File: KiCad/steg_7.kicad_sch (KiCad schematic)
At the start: 16 parts, among them U1 W65C02S, U2 LCD, U3 W65C22, U4 74HC00

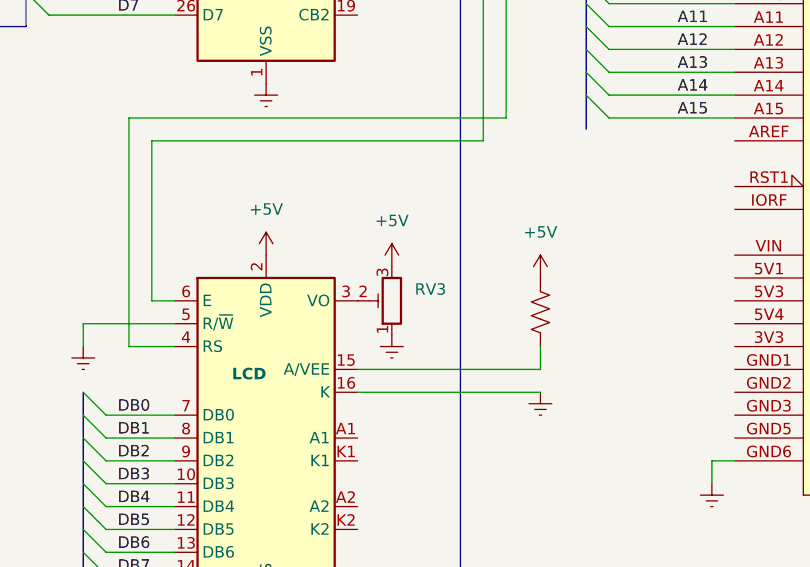
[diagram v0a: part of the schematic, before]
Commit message: Revert "Add trim potentiometer symbol and update power symbols in schematics"
This reverts commit c4bb345892a428583a00d61d4c040ffcc3a1eb40.
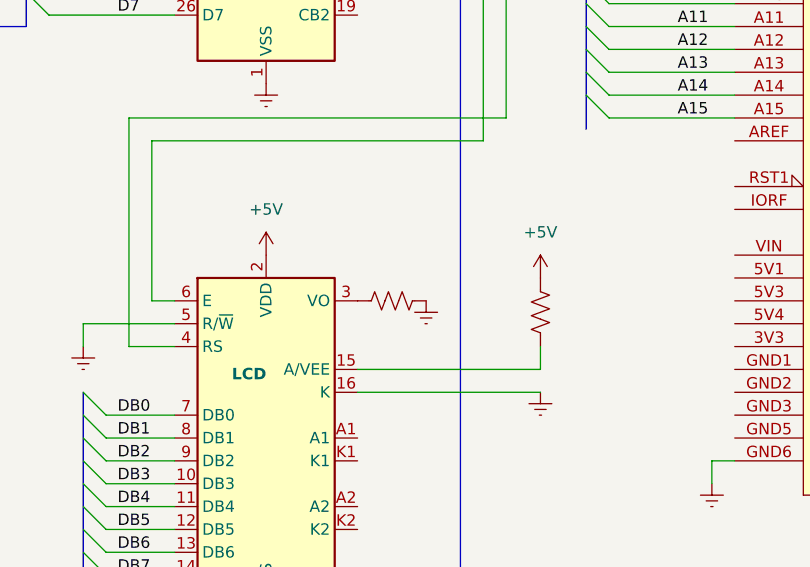
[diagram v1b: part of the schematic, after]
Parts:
- removed RV3: R_Potentiometer_Trim, symbol Device:R_Potentiometer_Trim
- added R7: (no value), symbol Device:R_US
- R6: value 220 -> (none)
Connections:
- net Earth: now also R7.2
- net at U2.3 (VO): now also R7.1

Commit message: Add trim potentiometer symbol and update power symbols in schematics
- Introduced a new trim potentiometer symbol (Device:R_Potentiometer_Trim) with properties for reference, value, footprint, and simulation details.
- Updated existing power symbols for +5V and Earth, including new references and descriptions.
- Adjusted positions and properties of various components in the schematic to enhance clarity and organization.
- Updated multiple schematic images to reflect the latest changes.
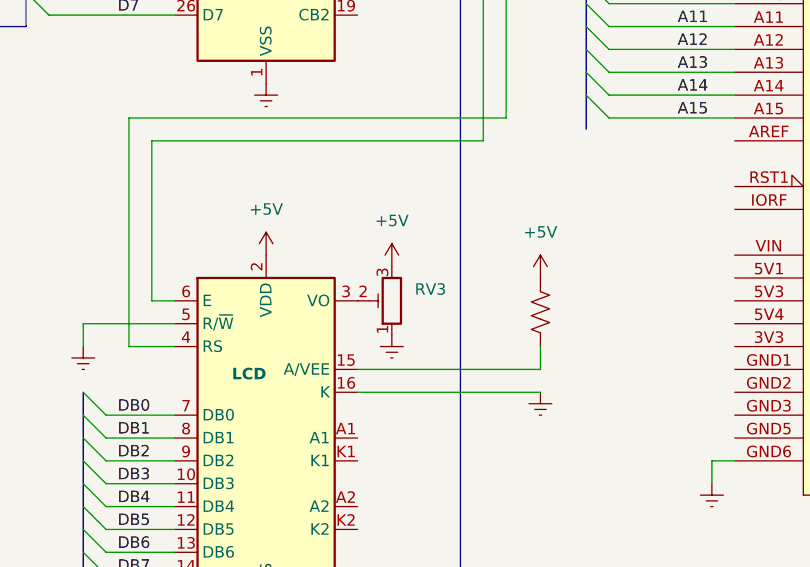
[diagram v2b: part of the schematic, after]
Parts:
- removed R7: (no value), symbol Device:R_US
- added RV3: R_Potentiometer_Trim, symbol Device:R_Potentiometer_Trim
- R6: value (none) -> 220
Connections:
- net +5V: now also RV3.3
- net Earth: now also RV3.1
- net at U2.3 (VO): now also RV3.2
